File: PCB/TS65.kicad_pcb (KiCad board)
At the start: 2 copper layers, 299.5 x 105.8 mm, 434 parts, among them P1 USB_CONN, P11 2PIN, P12 2PIN, P13 2PIN, P15 2PIN, P2 USB3, P3 USB3_MICRO, P4 6PIN, P5 6PIN, P6 ISP6, P7_1 5PIN, P7_2 5PIN, U1 Atmega32u4, U2 MCP23018, U3 IP4234CZ6, U4 74HC138, U5 PAM2804, X1 CRYSTAL

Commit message: Rev 0.7
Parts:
- removed R36: 1k, prettylib:SMD_0805
- added BREAKHOLES3: MISC, prettylib:BreakHoles, F.Cu at (213.8, 170.8)
- added BREAKHOLES4: MISC, prettylib:BreakHoles, F.Cu at (221.7, 170.8)
- JP1: footprint prettylib:JUMPER_SMD_2 -> prettylib:JUMPER_SMD_3
- R9: value 100k -> 10k
- moved R9 1.65 mm to (135.5, 85.5), turned to 0 degrees
- moved JP1 1.50 mm to (135.1, 88.2)
- moved BREAKHOLES1 1.13 mm to (208.8, 82.6)
- moved BREAKHOLES2 1.13 mm to (214.8, 82.6)
- moved FID8 1.02 mm to (224.4, 168.3)
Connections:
- JP1 pad 1: Net-(JP1-Pad1) -> +5V
- JP1 pad 2: /mcu/HWBE -> VSS
- R9 pad 1: /mcu/HWBE -> VSS
- R9 pad 2: +5V -> /mcu/HWBE
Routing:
- net +5V: track 1275.8 -> 1279.5 mm
- net VSS: track 1172.2 -> 1175.8 mm
- net /mcu/HWBE: track 17.3 -> 14.1 mm
- net Net-(JP1-Pad1): track 2.33 -> 0.00 mm
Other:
- outline, holes or cut-outs redrawn
- board text added: "TS65-L Rev 0.7 Designed & Drawn in KiCAD by Mohit 'MOZ' Garg"
- board text added: "TS65-R Rev 0.7 Designed & Drawn in KiCAD by Mohit 'MOZ' Garg"
- board text removed: "TS65-L Rev 0.6 Designed & Drawn in KiCAD by Mohit 'MOZ' Garg"
- board text removed: "TS65-R Rev 0.6 Designed & Drawn in KiCAD by Mohit 'MOZ' Garg"

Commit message: Rev 0.7
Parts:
- turned JP1 to 180 degrees
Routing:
- net +5V: track 1279.5 -> 1276.4 mm
- net VSS: track 1175.8 -> 1176.6 mm
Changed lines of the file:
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@@
   )
   (module prettylib:JUMPER_SMD_3 (layer Back)
-    (at 135.1407 88.2269)
-    (fp_text reference JP1 (at 0.0635 1.8288) (layer B.SilkS)
+    (at 135.1407 88.2269 180)
+    (fp_text reference JP1 (at -0.1143 -1.8161 180) (layer B.SilkS)
       (effects (font (size 1 1) (thickness 0.25)) (justify mirror))
     )
-    (fp_text value JUMPER (at 0.254 -1.524) (layer Dwgs.User)
+    (fp_text value JUMPER (at 0.254 -1.524 180) (layer Dwgs.User)
       (effects (font (size 0.5 0.5) (thickness 0.1)))
     )
@@
     (fp_line (start 2.159 -1.016) (end -2.159 -1.016) (layer B.SilkS) (width 0.2))
     (fp_line (start -2.159 -1.016) (end -2.159 1.016) (layer B.SilkS) (width 0.2))
-    (pad 2 smd rect (at 0 0) (size 1 1.5) (layers Back B.Paste B.Mask)
+    (pad 2 smd rect (at 0 0 180) (size 1 1.5) (layers Back B.Paste B.Mask)
       (net 1 VSS))
-    (pad 1 smd rect (at -1.5 0 180) (size 1 1.5) (layers Back B.Paste B.Mask)
+    (pad 1 smd rect (at -1.5 0) (size 1 1.5) (layers Back B.Paste B.Mask)
       (net 68 +5V))
-    (pad 3 smd rect (at 1.5 0 180) (size 1 1.5) (layers Back B.Paste B.Mask)
+    (pad 3 smd rect (at 1.5 0) (size 1 1.5) (layers Back B.Paste B.Mask)
       (net 1 VSS))
   )
@@
   (gr_line (start 213.7 100.8) (end 205.8 100.8) (layer Edge.Cuts) (width 0.127))
   (gr_line (start 214.5 85.4) (end 214.5 100) (layer Edge.Cuts) (width 0.127))
-  (segment (start 136.6407 88.2269) (end 135.1407 88.2269) (width 0.3048) (layer Back) (net 1))
+  (segment (start 133.6407 88.2269) (end 135.1407 88.2269) (width 0.3048) (layer Back) (net 1))
+  (segment (start 133.6407 88.2269) (end 133.6407 87.1721) (width 0.3048) (layer Back) (net 1))
+  (segment (start 133.6407 87.1721) (end 131.736399 85.267799) (width 0.3048) (layer Back) (net 1))
+  (segment (start 131.736399 85.267799) (end 131.622799 85.267799) (width 0.3048) (layer Back) (net 1))
+  (segment (start 131.622799 85.267799) (end 131.318 84.963) (width 0.3048) (layer Back) (net 1))
   (segment (start 135.1407 88.2269) (end 135.1407 86.1535) (width 0.3048) (layer Back) (net 1))
   (segment (start 135.1407 86.1535) (end 134.4963 85.5091) (width 0.3048) (layer Back) (net 1))
-  (segment (start 131.749052 84.963) (end 131.318 84.963) (width 0.3048) (layer Back) (net 1))
-  (segment (start 133.1454 84.963) (end 131.749052 84.963) (width 0.3048) (layer Back) (net 1))
-  (segment (start 133.6915 85.5091) (end 133.1454 84.963) (width 0.3048) (layer Back) (net 1))
-  (segment (start 134.4963 85.5091) (end 133.6915 85.5091) (width 0.3048) (layer Back) (net 1))
   (segment (start 128.397 85.612212) (end 102.728788 85.612212) (width 0.3048) (layer Back) (net 1))
   (segment (start 131.318 84.963) (end 131.013201 85.267799) (width 0.3048) (layer Back) (net 1))
@@
   (segment (start 154.305 118.475) (end 162.420253 118.475) (width 0.1524) (layer Back) (net 67))
   (segment (start 162.420253 118.475) (end 164.338 120.392747) (width 0.1524) (layer Back) (net 67))
-  (segment (start 133.6407 88.2269) (end 133.6407 89.5209) (width 0.3048) (layer Back) (net 68))
-  (segment (start 134.5184 90.3986) (end 137.1854 90.3986) (width 0.3048) (layer Back) (net 68))
-  (segment (start 133.6407 89.5209) (end 134.5184 90.3986) (width 0.3048) (layer Back) (net 68))
+  (segment (start 138.049 89.535) (end 137.6988 89.535) (width 0.3048) (layer Back) (net 68))
+  (segment (start 137.6988 89.535) (end 136.6407 88.4769) (width 0.3048) (layer Back) (net 68))
+  (segment (start 136.6407 88.4769) (end 136.6407 88.2269) (width 0.3048) (layer Back) (net 68))
   (segment (start 135.366 92.218) (end 137.1854 90.3986) (width 0.3048) (layer Back) (net 68))
   (segment (start 137.1854 90.3986) (end 138.049 89.535) (width 0.3048) (layer Back) (net 68))
@@
       )
     )
+  )
+  (zone (net 0) (net_name "") (layer Back) (hatch edge 0.508)
+    (connect_pads (clearance 0.308))
+    (min_thickness 0.254)
+    (keepout (tracks allowed) (vias allowed) (copperpour not_allowed))
+    (fill (arc_segments 16) (thermal_gap 0.508) (thermal_bridge_width 0.508))
+    (polygon
+      (pts
+        (xy 133.096 89.408) (xy 137.16 89.408) (xy 137.16 84.328) (xy 133.096 84.328)
+      )
+    )

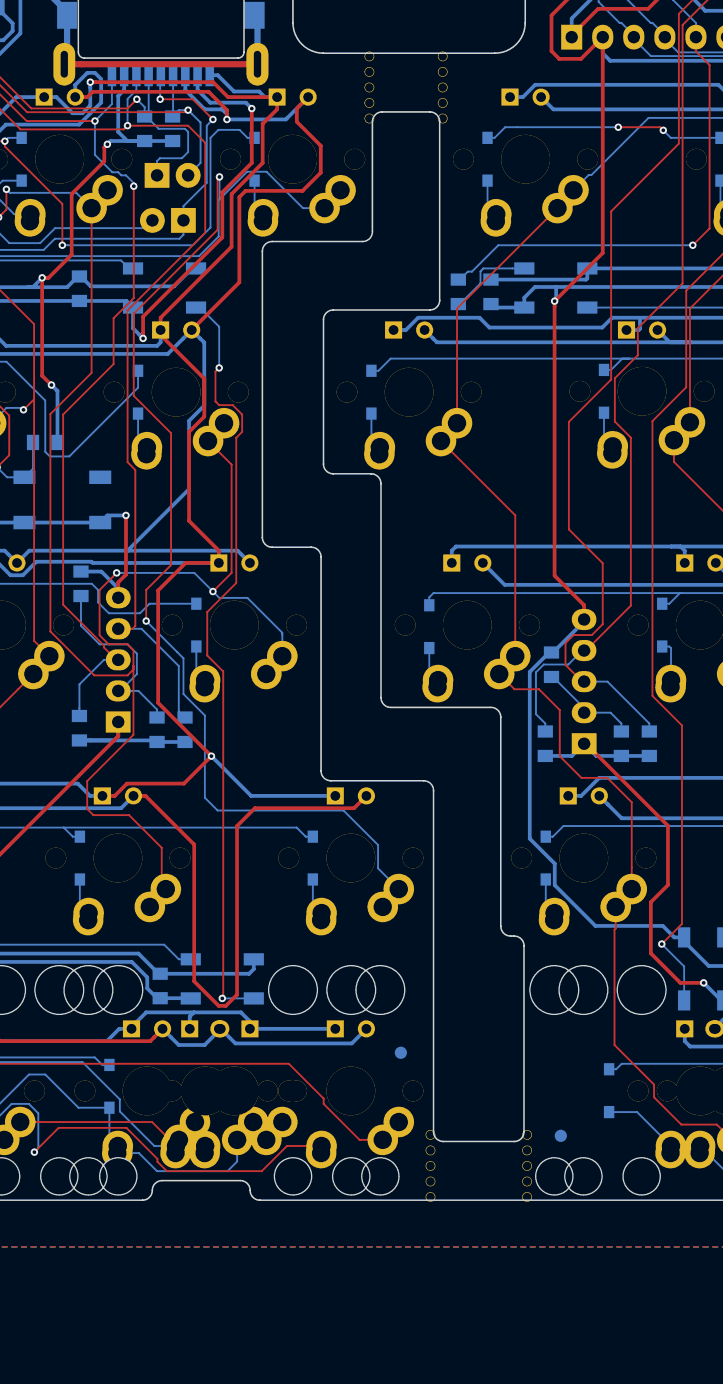
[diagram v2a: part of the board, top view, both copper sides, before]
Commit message: 0.7.1
- Corrected pin mappings for right half connector
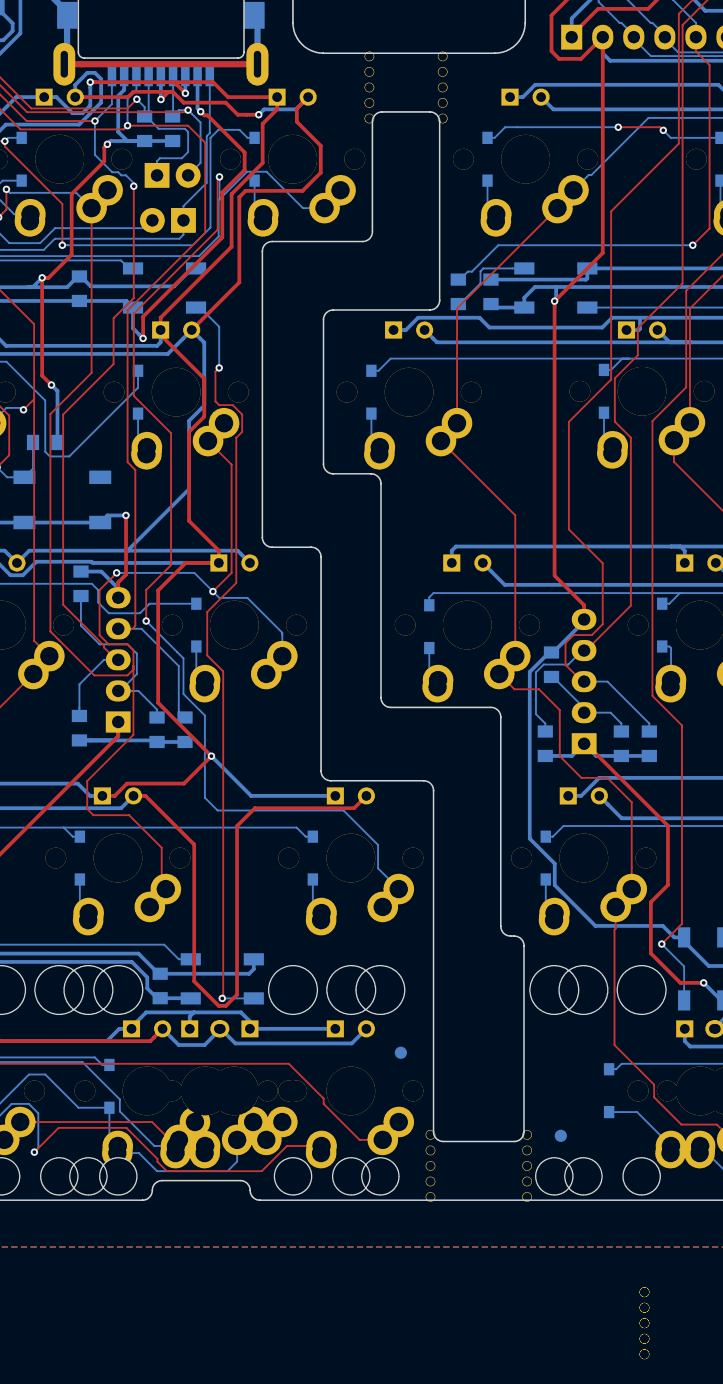
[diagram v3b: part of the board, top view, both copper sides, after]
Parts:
- added BREAKHOLES5, BREAKHOLES6: MISC, prettylib:BreakHoles, F.Cu at (231.2, 183.7)
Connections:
- net /mcu/COL1 renamed /Col1
- net /mcu/COL10 renamed /Col10
- net /mcu/COL11 renamed /Col11
- net /mcu/COL12 renamed /Col12
- net /mcu/COL13 renamed /Col13
- net /mcu/COL14 renamed /Col14
- net /mcu/COL15 renamed /Col15
- net /mcu/COL16 renamed /Col16
- net /mcu/COL2 renamed /Col2
- net /mcu/COL3 renamed /Col3
- net /mcu/COL4 renamed /Col4
- net /mcu/COL5 renamed /Col5
- net /mcu/COL6 renamed /Col6
- net /mcu/COL7 renamed /Col7
- net /mcu/COL8 renamed /Col8
- net /mcu/COL9 renamed /Col9
- net /mcu/ROWL1 renamed /RowL1
- net /mcu/ROWL2 renamed /RowL2
- net /mcu/ROWL3 renamed /RowL3
- net /mcu/ROWL4 renamed /RowL4
- net /mcu/ROWL5 renamed /RowL5
- net /mcu/ROWR1 renamed /RowR1
- net /mcu/ROWR2 renamed /RowR2
- net /mcu/ROWR3 renamed /RowR3
- net /mcu/ROWR4 renamed /RowR4
- net /mcu/ROWR5 renamed /RowR5
- P1 pad 4: (no net) -> Net-(P1-Pad4)
- P2 pad 5: /ledmatrix/LEDAN -> /ledmatrix/RGBLDOUT
- P2 pad 6: /ledmatrix/LEDCATH -> /ledmatrix/LEDAN
- P2 pad 7: /ledmatrix/RGBLDOUT -> /ledmatrix/LEDCATH
- P3 pad 4: (no net) -> Net-(P3-Pad4)
- S1 pad 1: (no net) -> Net-(S1-Pad1)
- U2 pad 15: (no net) -> Net-(U2-Pad15)
- U2 pad 16: (no net) -> Net-(U2-Pad16)
- U2 pad 8: (no net) -> Net-(U2-Pad8)
- U2 pad 9: (no net) -> Net-(U2-Pad9)
- U4 pad 7: (no net) -> Net-(U4-Pad7)
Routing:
- net /ledmatrix/RGBLDOUT: track 208.3 -> 204.7 mm, vias 4 -> 2
- net /ledmatrix/LEDCATH: track 781.4 -> 778.0 mm, vias 4 -> 5
- net /ledmatrix/LEDAN: track 738.9 -> 735.6 mm, vias 4 -> 5
- net VSS: track 1176.6 -> 1174.6 mm
